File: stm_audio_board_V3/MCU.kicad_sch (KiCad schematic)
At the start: 41 parts, among them J10 USB_A, SW1 SW_SPST, U1 IS42S16100H-7TL, U16 USBLC6-2P6, U17 W25Q128JVS, U19 FE1.1s, U7 STM32H723ZGTx, Y2 X1E0000210132, Y3 Crystal_GND24

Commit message: PCB design is finished
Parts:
- added R19 (x2): 3k, Resistor_SMD:R_0603_1608Metric, symbol Device:R
- renumbered D3 to DSP_OK1
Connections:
- net +3.3V: now also R19.1, R19.1
- net DSP_OK_LED: now also U7.90 (PG5); no longer U7.81 (PD12)
- net EXT_POT_ADC: now reaches U7.36 (PA2)
- net I2C_SDA: now reaches U7.82 (PD13)
- net I2C_SDA: now also R19.2
- new net I2C_SCL: R19.2, U7.81 (PD12)

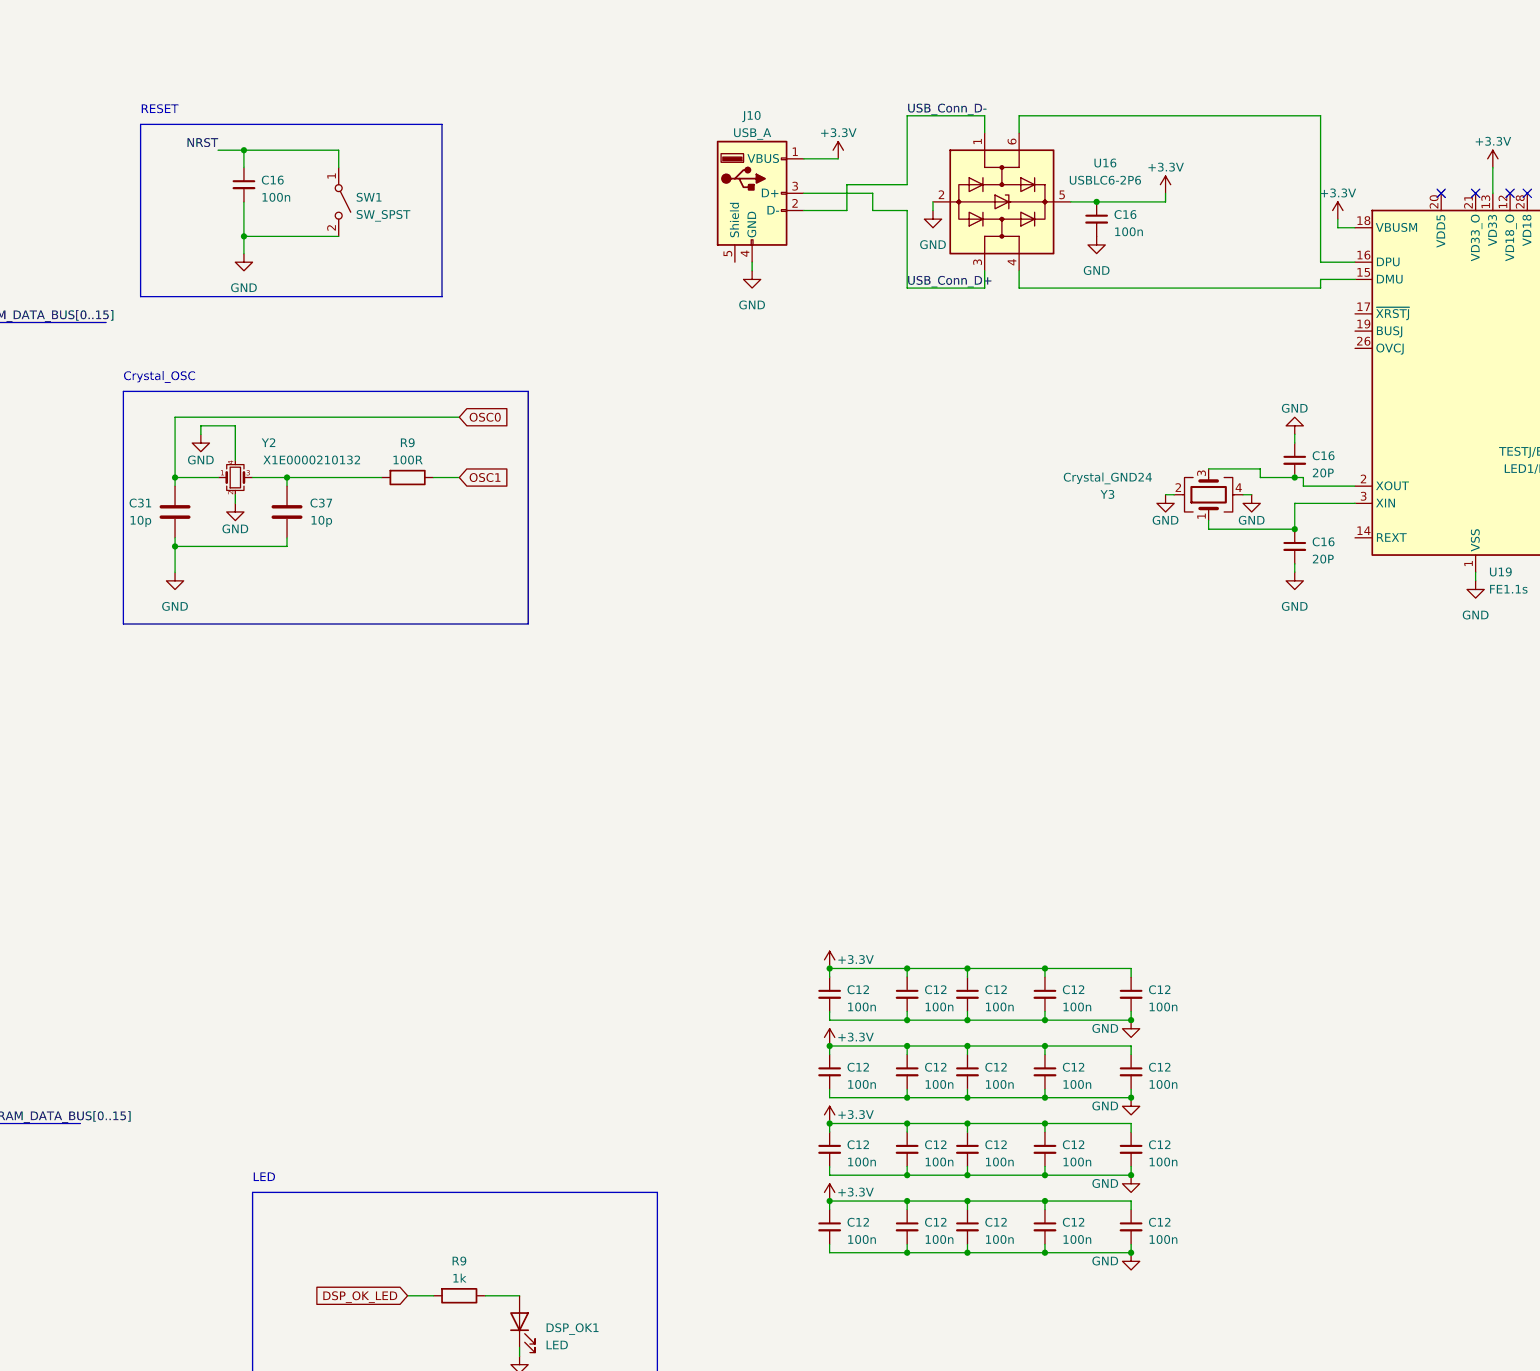
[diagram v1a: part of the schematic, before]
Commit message: minor changes to components
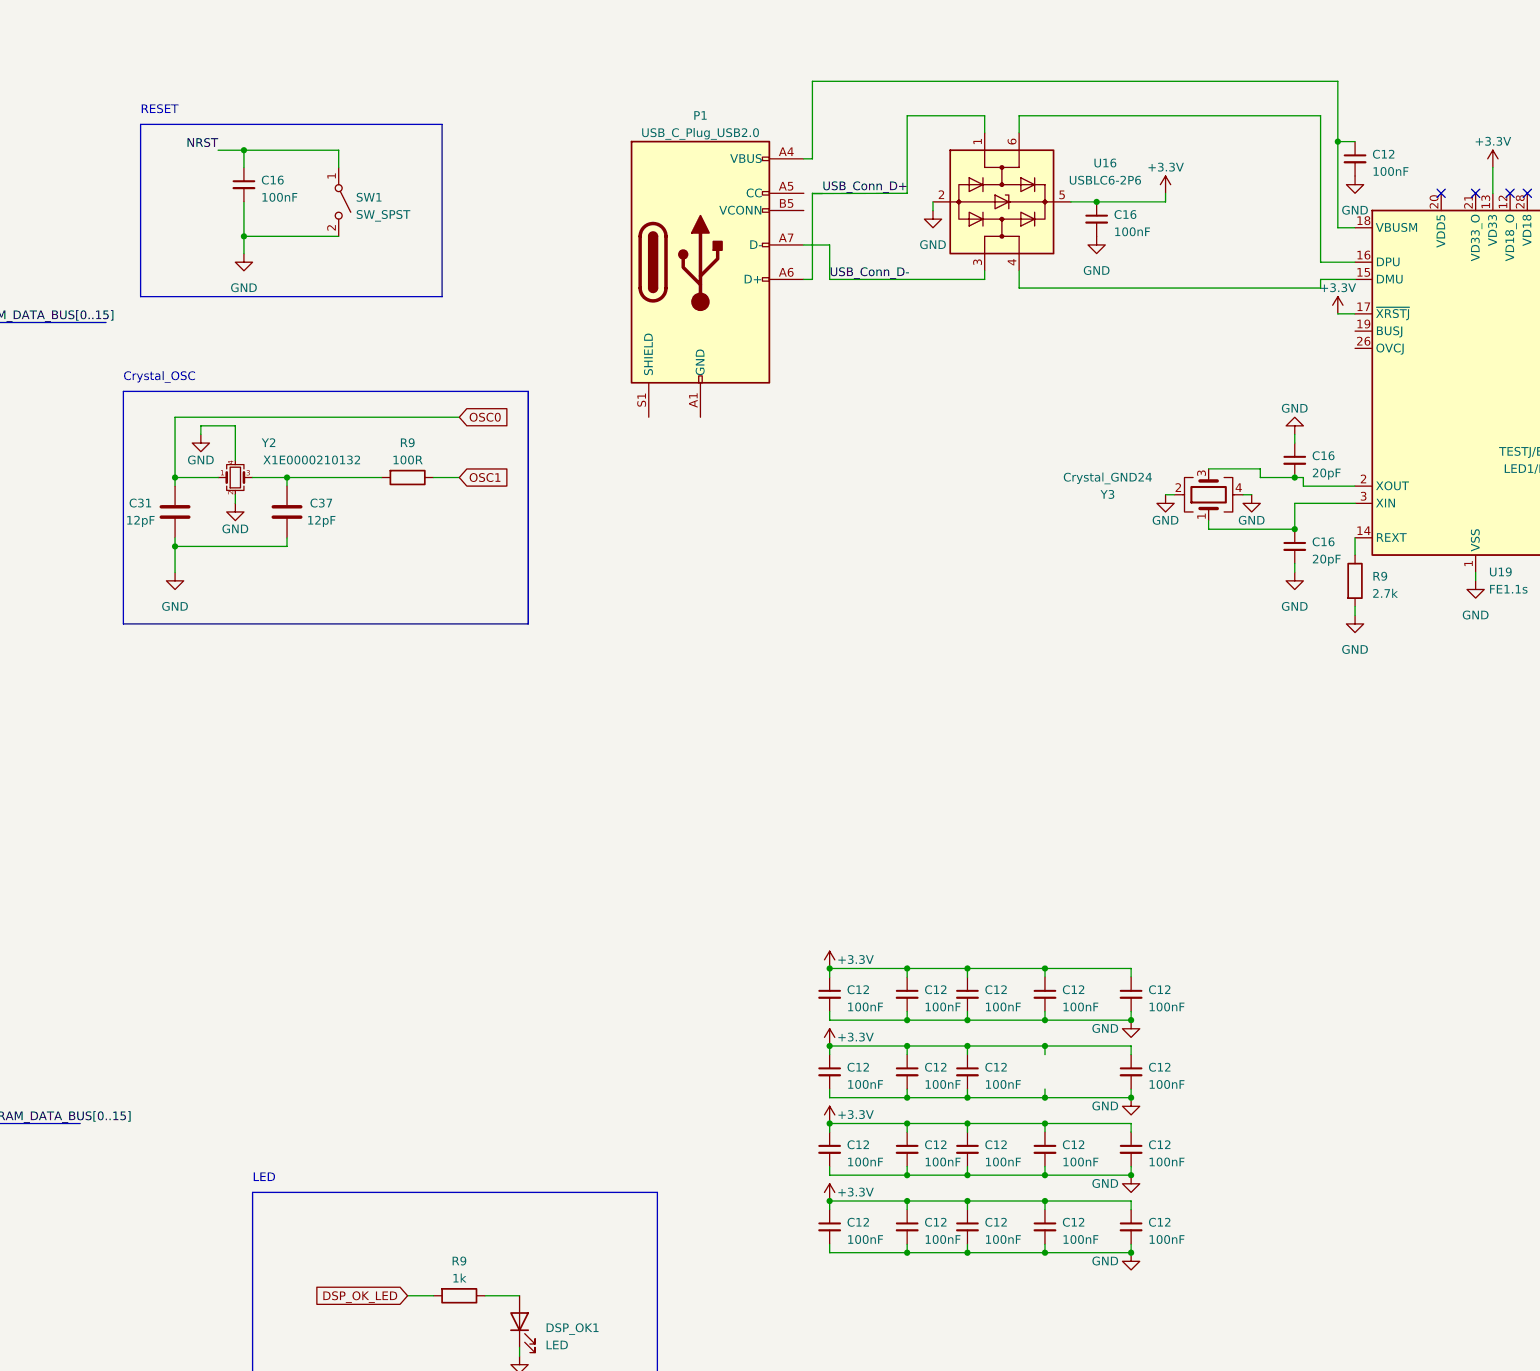
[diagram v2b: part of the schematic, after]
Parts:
- removed J10: USB_A, Connector_USB:USB_A_CONNFLY_DS1095-WNR0, symbol Connector:USB_A
- added P1: USB_C_Plug_USB2.0, Connector_USB:USB_C_Receptacle_XKB_U262-16XN-4BVC11, symbol Connector:USB_C_Plug_USB2.0
- added R9: 2.7k, Resistor_SMD:R_0603_1608Metric, symbol Device:R
- C12, C16: value 100n -> 100nF; JLCPCB (none) -> C14663; LCSC Part (none) -> C14663
- C15: JLCPCB (none) -> C377773; LCSC Part (none) -> C377773
- C16: value 20P -> 20pF; LCSC Part (none) -> C1554
- C31, C37: value 10p -> 12pF; JLCPCB (none) -> C38523; LCSC Part (none) -> C38523
- DSP_OK1: LCSC Part (none) -> C2297
- R19: JLCPCB (none) -> C4211; LCSC Part (none) -> C4211
- R2: JLCPCB (none) -> C25804; LCSC Part (none) -> C25804
- R9: footprint Resistor_SMD:R_0603_1608Metric_Pad0.98x0.95mm_HandSolder -> Resistor_SMD:R_0603_1608Metric; JLCPCB (none) -> C21190; LCSC Part (none) -> C21190
- R9: JLCPCB (none) -> C22775; LCSC Part (none) -> C22775
- U1: LCSC Part (none) -> C150435
- U16: LCSC Part (none) -> C15999
- U17: JLCPCB (none) -> C97521; LCSC Part (none) -> C97521
- U19: JLCPCB (none) -> C9359; LCSC Part (none) -> C9359
- U7: LCSC Part (none) -> C730146
- Y2: LCSC Part (none) -> C9006
- Y3: LCSC Part (none) -> C9002
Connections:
- net +3.3V: now also U19.17 (~{XRSTJ}); no longer C12.1, U19.18 (VBUSM)
- net GND: now also R9.2
- net USB_Conn_D+: now also U16.1 (I/O1), P1.A6 (D+); no longer U16.3 (I/O2)
- net USB_Conn_D-: now also U16.3 (I/O2), P1.A7 (D-); no longer U16.1 (I/O1)
- net at U19.14 (REXT): now also R9.1
- new net: C12.1, P1.A4 (VBUS), P1.A9 (VBUS), P1.B4 (VBUS), P1.B9 (VBUS), U19.18 (VBUSM)
- new net: P1.A1 (GND), P1.A12 (GND), P1.B1 (GND), P1.B12 (GND)

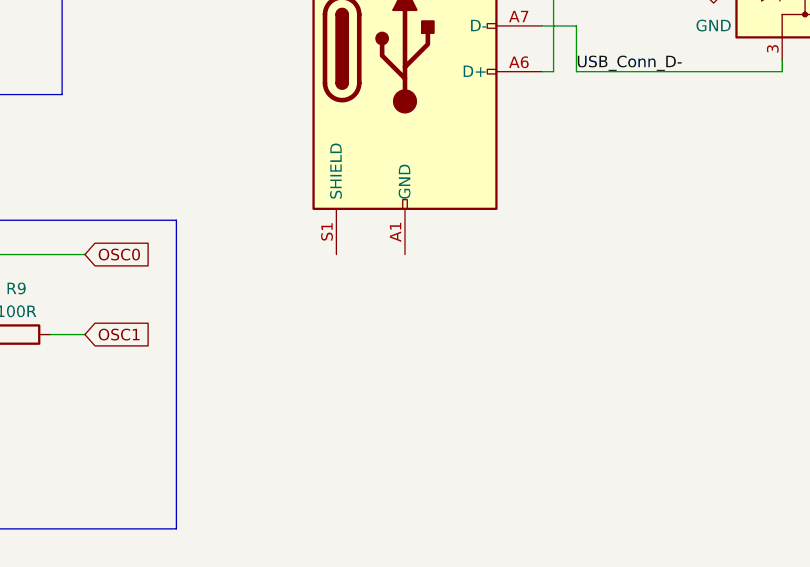
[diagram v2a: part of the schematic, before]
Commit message: added silkscreen captions, capacitor between gnd and earth
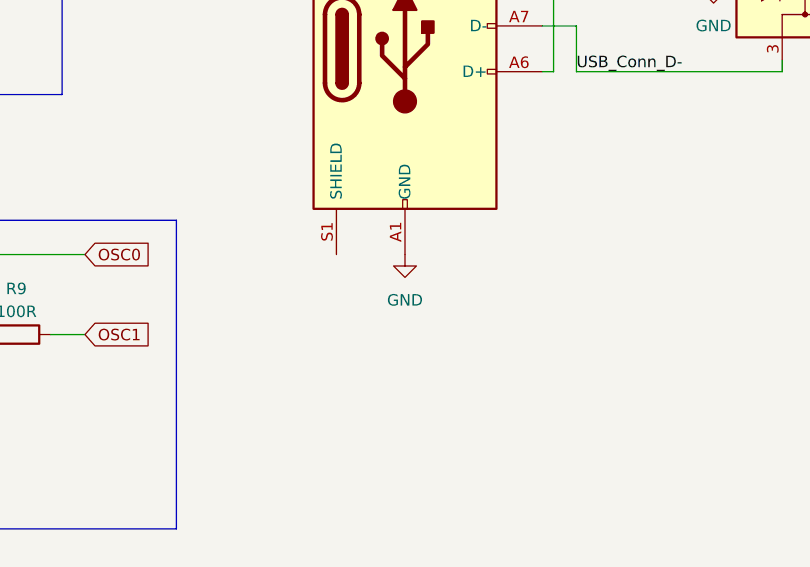
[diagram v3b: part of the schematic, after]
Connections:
- net GND: now also P1.A1 (GND), P1.A12 (GND), P1.B1 (GND), P1.B12 (GND)
